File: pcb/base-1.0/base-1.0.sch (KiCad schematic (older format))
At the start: 80 parts, among them J101 USB_B_Micro, J102 UART, J103 74984104400, J104 Jack-DC, J105 USB_GPIO, J106 Raspberry_Pi_2_3, Q101 BC817, Q102 BC817, Q103 DMP2305U-7, SW101 SW_Push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

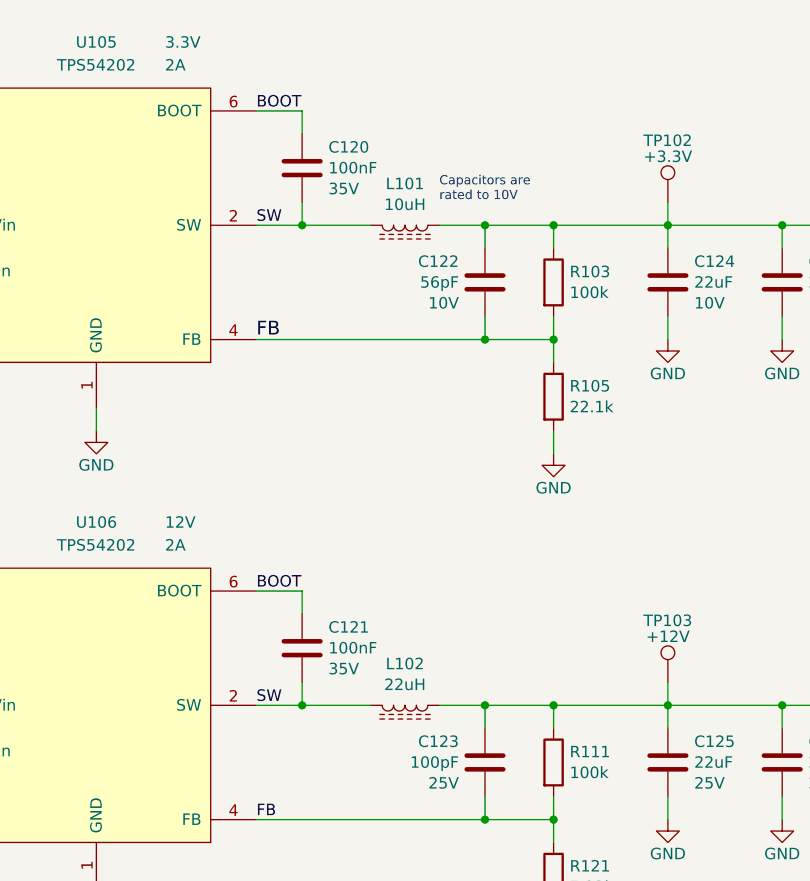
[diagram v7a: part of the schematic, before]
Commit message: o More part numbers.
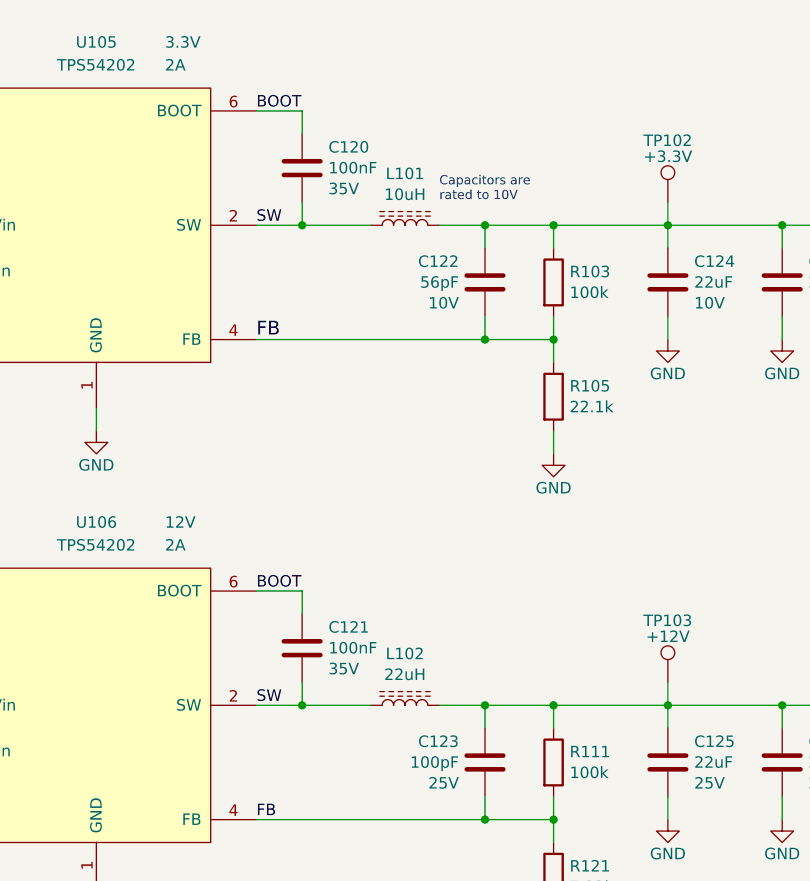
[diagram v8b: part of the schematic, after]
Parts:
- D103, D104: mpn (none) -> SML-P12VTT86R
- L101: footprint (none) -> Inductor_SMD:L_Taiyo-Yuden_NR-60xx; Imin (none) -> 2A; mpn (none) -> NR6045T100M
- L102: footprint (none) -> Inductor_SMD:L_Taiyo-Yuden_NR-80xx; Imin (none) -> NRS8040T220MJGJ
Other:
- moved on the sheet: L101, L102
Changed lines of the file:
@@
 	1    0    0    -1
-$EndComp
-$Comp
-L Device:L_Core_Ferrite L101
-U 1 1 5DDFE499
-P 13550 6600
-F 0 "L101" V 13369 6600 50  0000 C CNN
-F 1 "10uH" V 13460 6600 50  0000 C CNN
-F 2 "" H 13550 6600 50  0001 C CNN
-F 3 "" H 13550 6600 50  0001 C CNN
-F 4 "L1" V 13550 6600 50  0001 C CNN "ta_ref"
-	1    13550 6600
-	0    1    1    0
 $EndComp
 NoConn ~ 11500 6800
@@
 U 1 1 5DE430A1
 P 13550 8700
-F 0 "L102" V 13369 8700 50  0000 C CNN
-F 1 "22uH" V 13460 8700 50  0000 C CNN
-F 2 "" H 13550 8700 50  0001 C CNN
-F 3 "" H 13550 8700 50  0001 C CNN
+F 0 "L102" V 13775 8700 50  0000 C CNN
+F 1 "22uH" V 13684 8700 50  0000 C CNN
+F 2 "Inductor_SMD:L_Taiyo-Yuden_NR-80xx" H 13550 8700 50  0001 C CNN
+F 3 "https://ds.yuden.co.jp/TYCOMPAS/ut/detail?pn=NRS8040T220MJGJ%20%20&u=M" H 13550 8700 50  0001 C CNN
 F 4 "L1" V 13550 8700 50  0001 C CNN "ta_ref"
+F 5 "NRS8040T220MJGJ" V 13550 8700 50  0001 C CNN "Imin"
 	1    13550 8700
-	0    1    1    0
+	0    1    -1   0
 $EndComp
 $Comp
@@
 F 2 "IPC-7351-LEDSC:LEDSC_3216x060" H 7100 1950 50  0001 C CNN
 F 3 "~" H 7100 1950 50  0001 C CNN
-       1    7100 1950
-       0    -1   -1   0
+F 4 "SML-P12VTT86R" V 7100 1950 50  0001 C CNN "mpn"
+	1    7100 1950
+	0    -1   -1   0
 $EndComp
 Wire Wire Line
@@
 F 2 "IPC-7351-LEDSC:LEDSC_3216x060" H 7500 1950 50  0001 C CNN
 F 3 "~" H 7500 1950 50  0001 C CNN
+F 4 "SML-P12VTT86R" V 7500 1950 50  0001 C CNN "mpn"
 	1    7500 1950
 	0    -1   -1   0
@@
 	1    0    0    -1
 $EndComp
+$Comp
+L Device:L_Core_Ferrite L101
+U 1 1 5DDFE499
+P 13550 6600
+F 0 "L101" V 13775 6600 50  0000 C CNN
+F 1 "10uH" V 13684 6600 50  0000 C CNN
+F 2 "Inductor_SMD:L_Taiyo-Yuden_NR-60xx" H 13550 6600 50  0001 C CNN
+F 3 "https://www.yuden.co.jp/productdata/catalog/wound04_e.pdf" H 13550 6600 50  0001 C CNN
+F 4 "L1" V 13550 6600 50  0001 C CNN "ta_ref"
+F 5 "2A" V 13550 6600 50  0001 C CNN "Imin"
+F 6 "NR6045T100M" V 13550 6600 50  0001 C CNN "mpn"
+	1    13550 6600
+	0    1    -1   0
+$EndComp
 $EndSCHEMATC
